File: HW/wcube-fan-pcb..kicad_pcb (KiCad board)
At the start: 2 copper layers, 43 parts, among them J1 HOT_END, J2 ON_~OFF, J3 POWER, J4 AVR_ISP_02X03, M1 Fan, M2 Fan, M3 Fan, M4 Fan, Q1 BC817, Q2 BC817, Q3 BC817, Q4 BC807, Q5 BC807, Q6 BC807, U1 ATTINY13A-SSU, U2 L78L05_SO8

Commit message: Created layout
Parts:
- removed H3, H4: M3, KLIB_Mechanical:Bolt_M3
- removed J4: AVR_ISP_02X03, Connector_IDC:IDC-Header_2x03_P2.54mm_Vertical
- C1, C2, C3, C4, C5, C6, Q2, Q5, R10, R2, R5, R8, U1, U2: moved to B.Cu
- D1, D2, D3: value SS14 -> SS24; footprint Diode_SMD:D_SMA -> Diode_SMD:D_SMB_Handsoldering
- D4: value SS14 -> SS24; footprint Diode_SMD:D_SMA -> Diode_SMD:D_SMB_Handsoldering; moved to B.Cu
- moved Q1 97.7 mm to (88.8, 58.8), turned to 90 degrees
- moved Q4 89.3 mm to (93.5, 63.5)
- moved R1 88.8 mm to (82.5, 59.0), turned to 90 degrees
- moved R7 86.3 mm to (92.5, 59.0), turned to 90 degrees
- moved R10 85.8 mm to (97.8, 58.2), turned to 270 degrees
- moved R4 84.9 mm to (85.0, 59.0), turned to 90 degrees
- moved H1 82.5 mm to (88.2, 64.1)
- moved R2 80.3 mm to (102.8, 57.5), turned to 270 degrees
- moved Q2 80.1 mm to (108.2, 57.5), turned to 270 degrees
- moved R5 78.1 mm to (105.0, 57.5), turned to 90 degrees
- moved D1 74.8 mm to (99.0, 62.0), turned to 270 degrees
- moved Q5 71.6 mm to (116.5, 59.0), turned to 270 degrees
- moved R8 71.1 mm to (112.5, 58.0), turned to 180 degrees
- moved C2 71.0 mm to (108.0, 64.5), turned to 270 degrees
- moved J2 71.0 mm to (85.5, 53.9), turned to 180 degrees
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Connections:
- U1 pad 5: /PWM_HEAD -> /PWM_BOX
- U1 pad 6: /PWM_BOX -> /PWM_HEAD
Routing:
- net /PWM_BOX: track 0.00 -> 75.5 mm, vias 0 -> 1
- net +12V: track 0.00 -> 64.0 mm, vias 0 -> 2
- net /PWM_HEAD: track 0.00 -> 50.2 mm
- net +5V: track 0.00 -> 40.3 mm
- net Net-(D3-Pad1): track 0.00 -> 22.3 mm
- net Net-(D2-Pad1): track 0.00 -> 20.9 mm
- net /ADC_HEAD: track 0.00 -> 17.3 mm
- net /ON_~OFF: track 0.00 -> 17.0 mm
- net Net-(D1-Pad1): track 0.00 -> 15.0 mm
- net /PWM_HOT_END: track 0.00 -> 10.8 mm
- net /ADC_BOX: track 0.00 -> 10.4 mm
- net Net-(D4-Pad2): track 0.00 -> 7.47 mm
- net Net-(Q3-Pad3): track 0.00 -> 4.16 mm
- net Net-(Q2-Pad1): track 0.00 -> 3.85 mm
- net Net-(Q1-Pad3): track 0.00 -> 3.82 mm
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- added copper zone on B.Cu, net GND
- added copper zone on F.Cu, net GND
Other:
- board outline added: 60 x 17.5 mm
- net class Default: clearance 0.2 -> 0.25
- rule trace_clearance: 0.2 -> 0.25

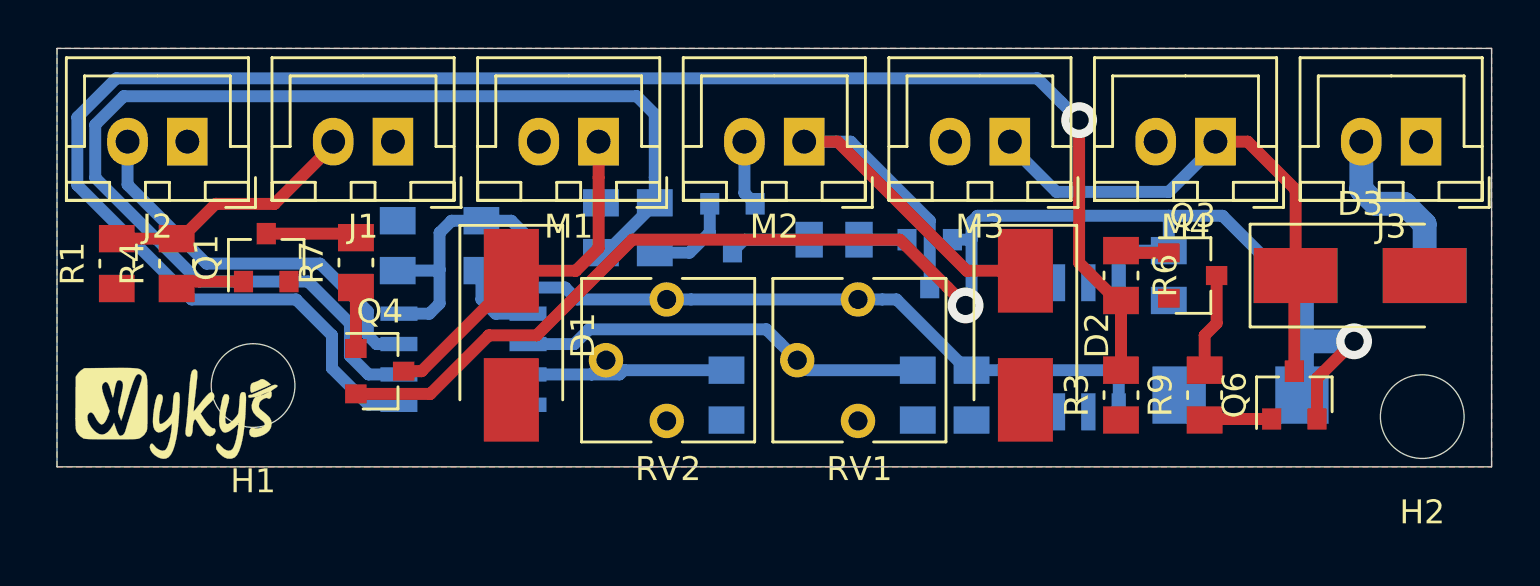
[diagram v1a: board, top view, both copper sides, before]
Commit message: Updated layout
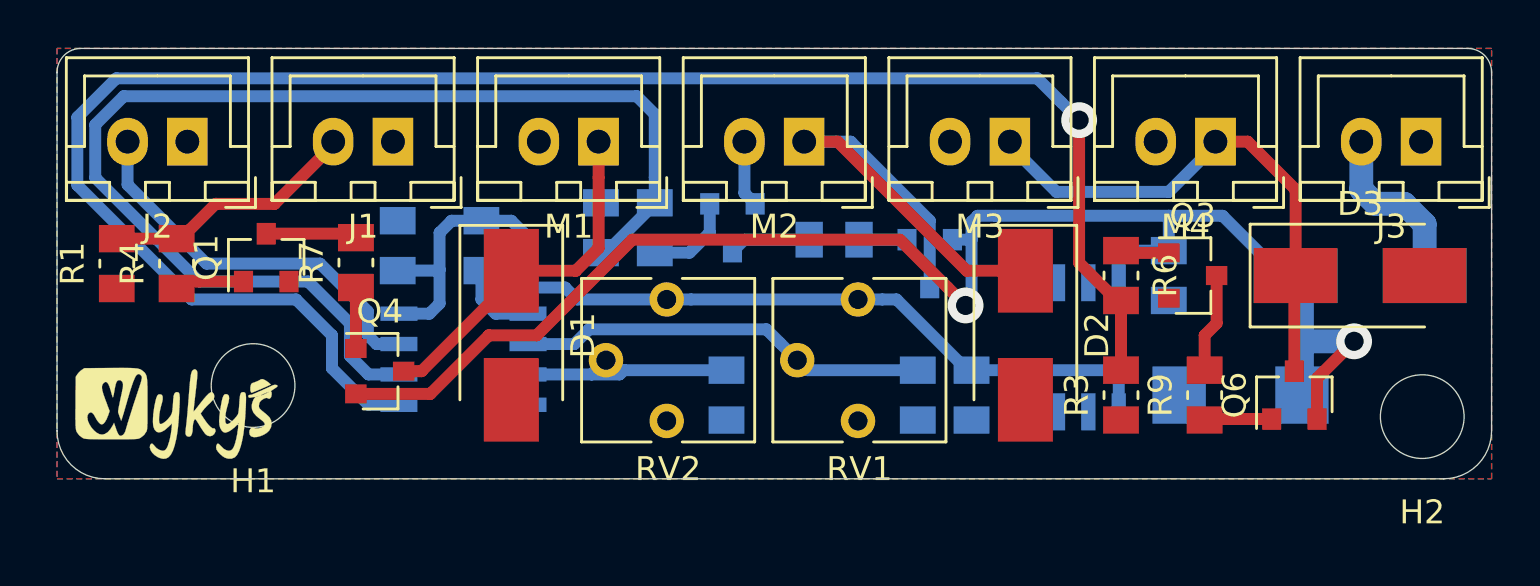
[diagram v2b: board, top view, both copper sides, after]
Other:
- board size 60 x 17.5 mm -> 60 x 18 mm
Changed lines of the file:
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@@
   (general
     (thickness 1.6)
-    (drawings 9)
+    (drawings 14)
     (tracks 167)
     (zones 0)
@@
     (38 B.Mask user)
     (39 F.Mask user)
-    (40 Dwgs.User user hide)
+    (40 Dwgs.User user)
     (41 Cmts.User user)
     (42 Eco1.User user)
@@
     )
   )
+  (dimension 18 (width 0.15) (layer Dwgs.User)
+    (gr_text "18,000 mm" (at 147.3 59 270) (layer Dwgs.User)
+      (effects (font (size 1 1) (thickness 0.15)))
+    )
+    (feature1 (pts (xy 140 68) (xy 146.586421 68)))
+    (feature2 (pts (xy 140 50) (xy 146.586421 50)))
+    (crossbar (pts (xy 146 50) (xy 146 68)))
+    (arrow1a (pts (xy 146 68) (xy 145.413579 66.873496)))
+    (arrow1b (pts (xy 146 68) (xy 146.586421 66.873496)))
+    (arrow2a (pts (xy 146 50) (xy 145.413579 51.126504)))
+    (arrow2b (pts (xy 146 50) (xy 146.586421 51.126504)))
+  )
+  (gr_arc (start 81 51) (end 81 50) (angle -90) (layer Edge.Cuts) (width 0.05))
+  (gr_arc (start 82 66) (end 80 66) (angle -90) (layer Edge.Cuts) (width 0.05))
+  (gr_arc (start 138 66) (end 138 68) (angle -90) (layer Edge.Cuts) (width 0.05))
+  (gr_arc (start 139 51) (end 140 51) (angle -90) (layer Edge.Cuts) (width 0.05))
   (dimension 8.2 (width 0.15) (layer Dwgs.User)
     (gr_text "8,200 mm" (at 84.1 73.3) (layer Dwgs.User)
@@
     (arrow2b (pts (xy 78 50) (xy 78.586421 51.126504)))
   )
-  (gr_line (start 80 67.5) (end 80 50) (layer Edge.Cuts) (width 0.05))
-  (gr_line (start 140 67.5) (end 80 67.5) (layer Edge.Cuts) (width 0.05))
-  (gr_line (start 140 50) (end 140 67.5) (layer Edge.Cuts) (width 0.05))
-  (gr_line (start 80 50) (end 140 50) (layer Edge.Cuts) (width 0.05))
+  (gr_line (start 80 66) (end 80 51) (layer Edge.Cuts) (width 0.05))
+  (gr_line (start 138 68) (end 82 68) (layer Edge.Cuts) (width 0.05))
+  (gr_line (start 140 51) (end 140 66) (layer Edge.Cuts) (width 0.05))
+  (gr_line (start 81 50) (end 139 50) (layer Edge.Cuts) (width 0.05))
   (segment (start 108.75 56.05) (end 109.2 56.5) (width 0.5) (layer B.Cu) (net 1))
   (segment (start 108.75 53.9) (end 108.75 56.05) (width 0.5) (layer B.Cu) (net 1))
@@
     (polygon
       (pts
-        (xy 80 50) (xy 80 67.5) (xy 140 67.5) (xy 140 50)
+        (xy 80 50) (xy 80 68) (xy 140 68) (xy 140 50)
       )
     )
@@
     (polygon
       (pts
-        (xy 140 67.5) (xy 140 50) (xy 80 50) (xy 80 67.5)
+        (xy 140 68) (xy 140 50) (xy 80 50) (xy 80 68)
       )
     )
